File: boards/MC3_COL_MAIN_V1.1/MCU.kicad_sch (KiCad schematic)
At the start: 52 parts, among them J2 SWD, SW1 SKRKAEE020, U10 GP1S094HCZ0F, U11 GP1S094HCZ0F, U2 STM32U595RJT6, U9 AEDR-8300-1Q0, Y1 8MHz

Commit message: V1.1: 24 V input - LM61460 sync buck (U12) + support, F1/D1/Q1 re-rated, D7 gate zener, BUCK_SYNC on PB4/LPTIM1_CH2, VIN24 netclass; ERC 0 errors
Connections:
- net BUCK_SYNC: now reaches U2.56 (PB4)
- no-connect marks 5 -> 4

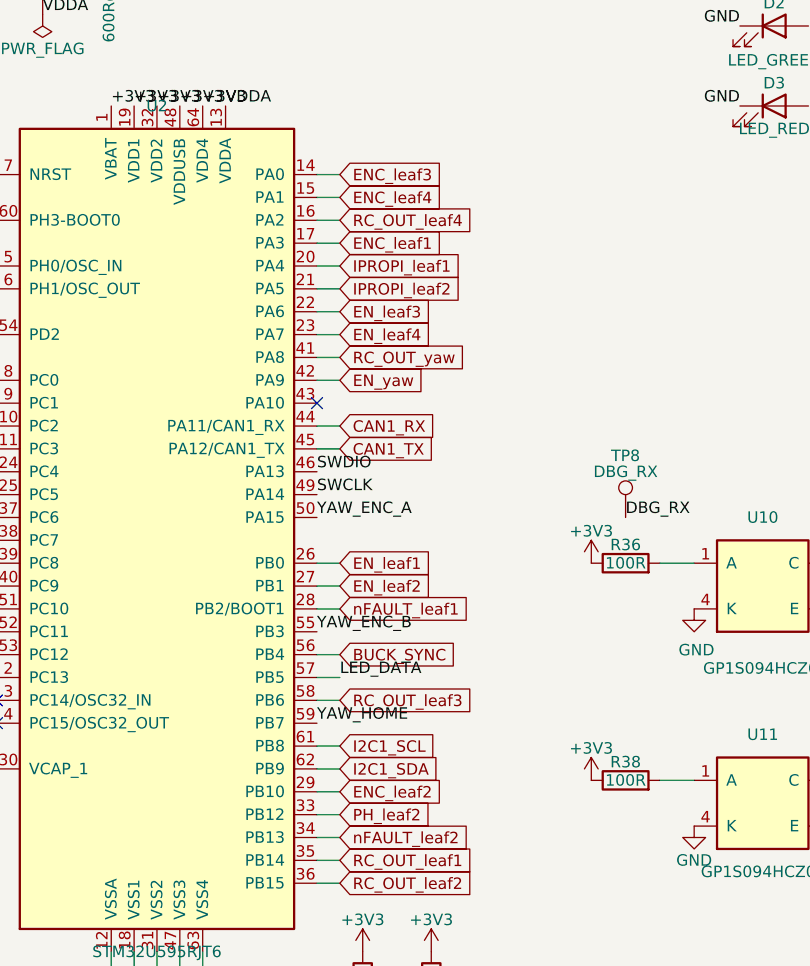
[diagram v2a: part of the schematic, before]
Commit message: V1.1: ENC rename carried to MCU labels (pure rename over existing copper); pinout + firmware pages updated
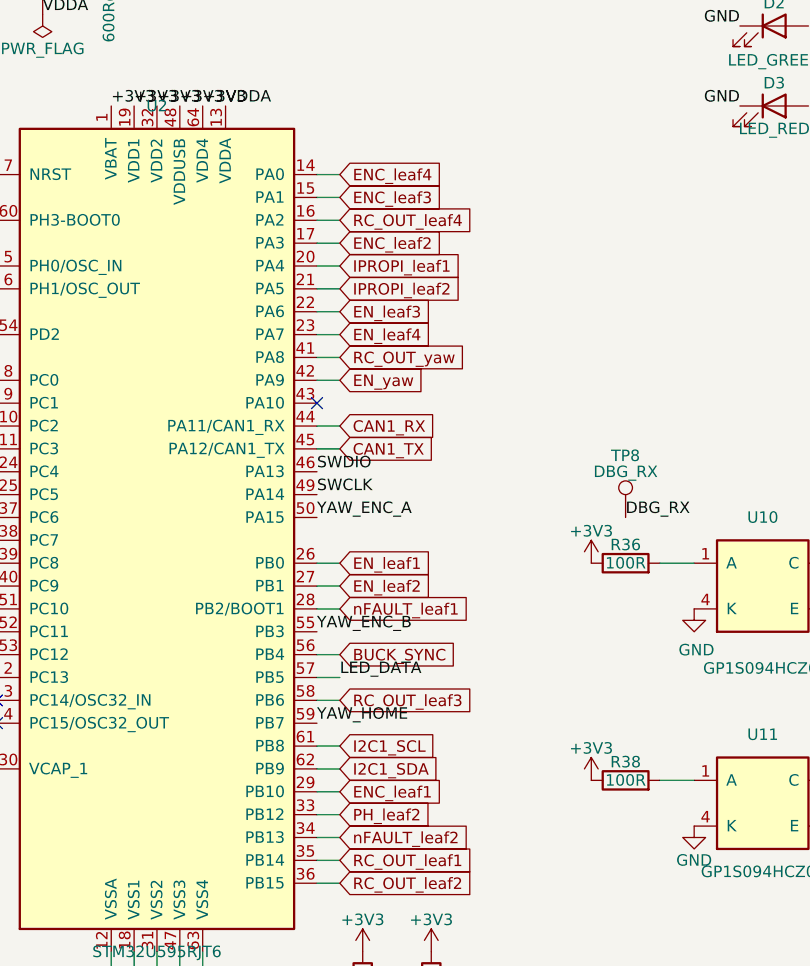
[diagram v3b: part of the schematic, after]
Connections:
- net ENC_leaf1: now also U2.29 (PB10); no longer U2.17 (PA3)
- net ENC_leaf2: now also U2.17 (PA3); no longer U2.29 (PB10)
- net ENC_leaf3: now also U2.15 (PA1); no longer U2.14 (PA0)
- net ENC_leaf4: now also U2.14 (PA0); no longer U2.15 (PA1)
